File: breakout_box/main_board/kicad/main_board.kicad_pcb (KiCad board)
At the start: 2 copper layers, 56 x 120 mm, 38 parts, among them CN1 19PIN_LEMO, Q1 DMP3099L, Q2 TIP122

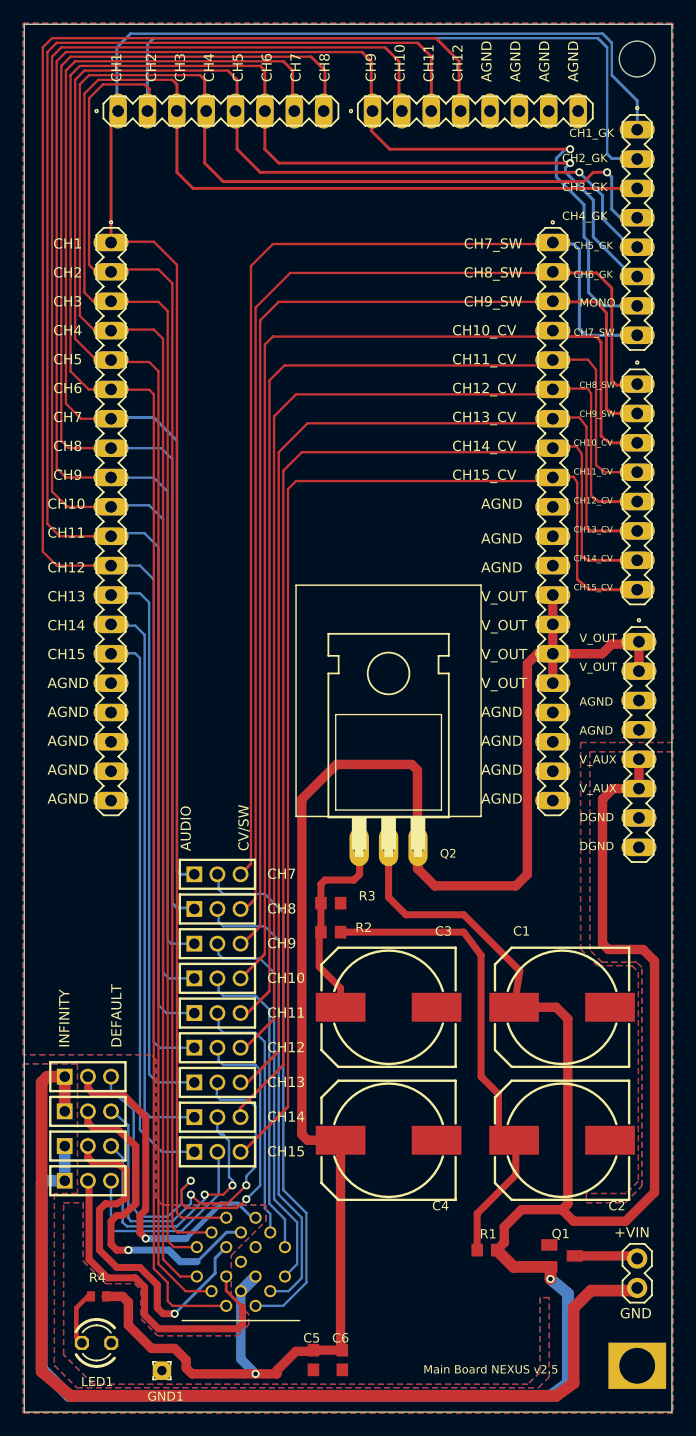
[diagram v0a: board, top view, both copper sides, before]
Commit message: Changed transistor to SMD type
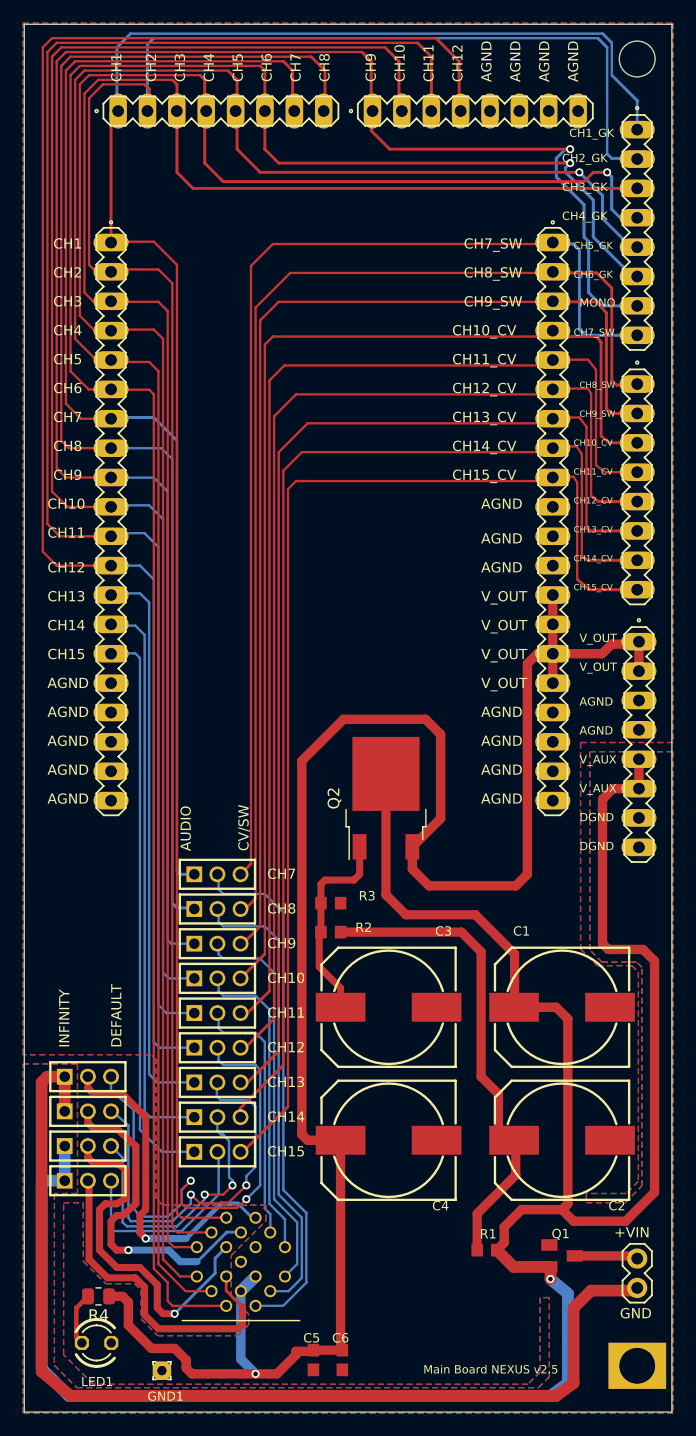
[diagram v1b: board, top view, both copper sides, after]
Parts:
- Q2: value TIP122 -> MJD122; footprint main_board:TO-220H -> Package_TO_SOT_SMD:TO-252-2
- R4: footprint main_board:R0402 -> Resistor_SMD:R_0805_2012Metric
- moved Q2 3.43 mm to (151.8, 111.9), turned to 90 degrees
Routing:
- net /V_OUT: track 157.7 -> 166.0 mm
- net /V_AUX: track 188.2 -> 195.0 mm

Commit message: Clean update for KiCad
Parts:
- removed GND1: TH-PAD-1.6/0.8, main_board:TH-PAD-1.6_0.8
- C5, C6: footprint main_board:C0603 -> Capacitor_SMD:C_0603_1608Metric
- H17, H3, H4, H7, H8: footprint main_board:MA08-1 -> Connector_PinHeader_2.54mm:PinHeader_1x08_P2.54mm_Vertical
- Q1: footprint main_board:SOT23 -> Package_TO_SOT_SMD:SOT-23
- R1, R2, R3: footprint main_board:R0603 -> Resistor_SMD:R_0603_1608Metric
- moved H4 9.00 mm to (150.5, 52.4), turned to 90 degrees
- moved H17 8.98 mm to (173.5, 54.0), turned to 0 degrees
- moved H3 8.90 mm to (128.6, 52.4), turned to 90 degrees
- moved H7 8.88 mm to (173.5, 76.1), turned to 0 degrees
- moved H8 8.86 mm to (173.5, 98.4), turned to 0 degrees
- moved Q1 0.10 mm to (166.9, 151.5), turned to 0 degrees
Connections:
- net Net-(CN1-PadP$1) renamed CH1
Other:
- board text added: "JLCJLCJLCJLC"

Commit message: Very clean port to KiCAD
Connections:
- net /V_AUX renamed V_AUX
- net /V_OUT renamed V_OUT
- net Net-(CN1-PadP$10) renamed CH10
- net Net-(CN1-PadP$11) renamed CH11
- net Net-(CN1-PadP$12) renamed CH12
- net Net-(CN1-PadP$13) renamed CH13
- net Net-(CN1-PadP$14) renamed CH14
- net Net-(CN1-PadP$15) renamed CH15
- net Net-(CN1-PadP$2) renamed CH2
- net Net-(CN1-PadP$3) renamed CH3
- net Net-(CN1-PadP$4) renamed CH4
- net Net-(CN1-PadP$5) renamed CH5
- net Net-(CN1-PadP$6) renamed CH6
- net Net-(CN1-PadP$7) renamed CH7
- net Net-(CN1-PadP$8) renamed CH8
- net Net-(CN1-PadP$9) renamed CH9
- net Net-(H1-Pad1) renamed CH7_SW
- net Net-(H1-Pad2) renamed CH8_SW
- net Net-(H1-Pad3) renamed CH9_SW
- net Net-(H1-Pad4) renamed CH10_CV
- net Net-(H1-Pad5) renamed CH11_CV
- net Net-(H1-Pad6) renamed CH12_CV
- net Net-(H1-Pad7) renamed CH13_CV
- net Net-(H1-Pad8) renamed CH14_CV
- net Net-(H1-Pad9) renamed CH15_CV
- net Net-(H17-Pad7) renamed CH9_A
- net Net-(H2-Pad10) renamed CH10_A
- net Net-(H2-Pad11) renamed CH11_A
- net Net-(H2-Pad12) renamed CH12_A
- net Net-(H2-Pad13) renamed CH13_A
- net Net-(H2-Pad14) renamed CH14_A
- net Net-(H2-Pad15) renamed CH15_A
- net Net-(H2-Pad7) renamed CH7_A
- net Net-(H2-Pad8) renamed CH8_A
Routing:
- net CH7_SW: track 94.2 -> 90.4 mm
- net CH9_SW: track 96.6 -> 93.0 mm
- net CH10_CV: track 95.7 -> 92.2 mm
- net CH8_SW: track 95.0 -> 92.1 mm
- net CH11_CV: track 96.8 -> 94.1 mm
- net CH12_CV: track 96.6 -> 94.5 mm
- net CH14_CV: track 97.5 -> 96.3 mm
- net CH13_CV: track 97.0 -> 95.8 mm
- net CH15_CV: track 98.0 -> 96.8 mm
- net GND: vias 0 -> 76
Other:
- board text added: "Main Board NEXUS v2.51"
- board text removed: "Main Board NEXUS v2.5"

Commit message: PCB bug fix updates
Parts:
- added @HOLE0: , , F.Cu at (173.5, 122.0)
- added G***: LOGO, cycfi_library:cycfi-logo-15mm, F.Cu at (159.4, 159.7)
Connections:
- GND_HOLE pad : (no net) -> GND
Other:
- board text added: "Main Board Nexus v2.51"
- board text removed: "Main Board NEXUS v2.51"
